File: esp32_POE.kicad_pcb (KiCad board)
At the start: 2 copper layers, 204.8 x 25 mm, 68 parts, among them IC1 TPS2373-4RGWR, J1 USB_C_Receptacle_USB2.0_14P, J10 Conn_01x02, J2 WE-RJ45LAN 10/100BaseT PoE, J3 Screw_Terminal_01x03, J4 Screw_Terminal_01x03, J5 Screw_Terminal_01x03, J6 Screw_Terminal_01x03, J7 Conn_01x04, J8 Conn_01x02, J9 Conn_01x04, Q1 NPN, Q2 NPN, SW1 SW_Push, U1 ESP32-WROOM-32E, U2 CH340C, U4 LAN8710A, U5 AMS1117-3.3, U7 TXS0108EPW

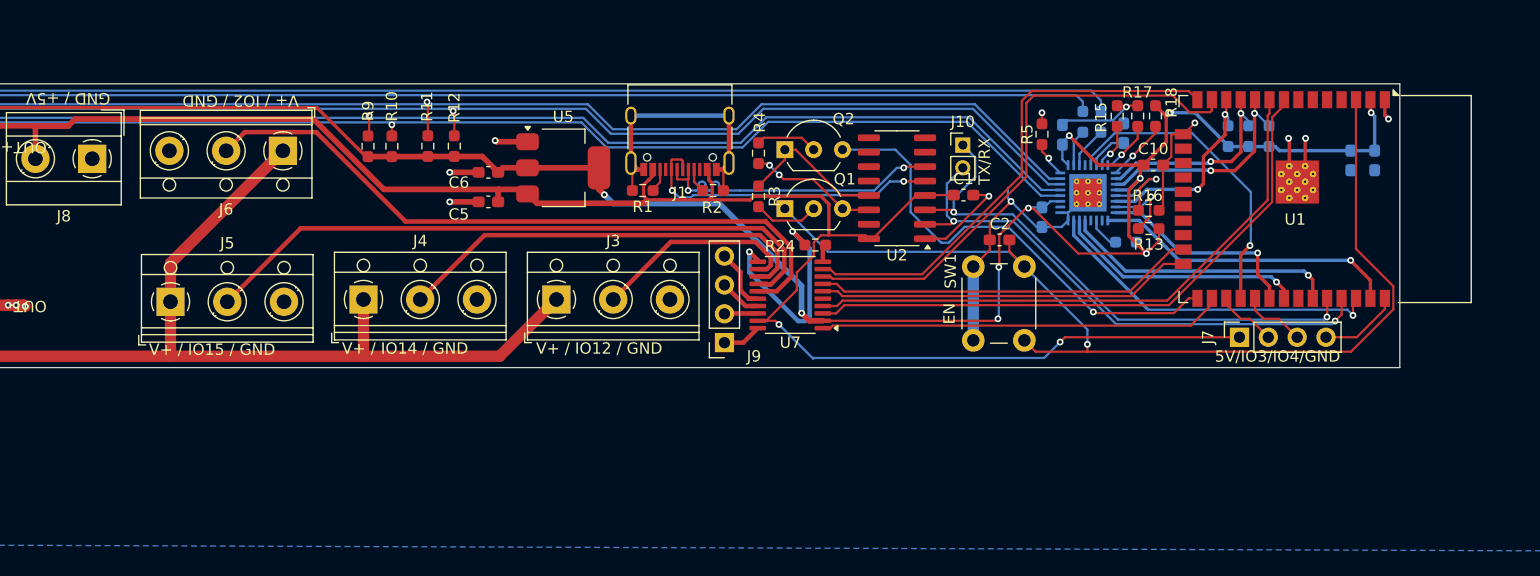
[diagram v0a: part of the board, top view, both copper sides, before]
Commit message: Modified schematic : fixed esp32 circuit, changed to SN74 level shifter, changed to LAN8270
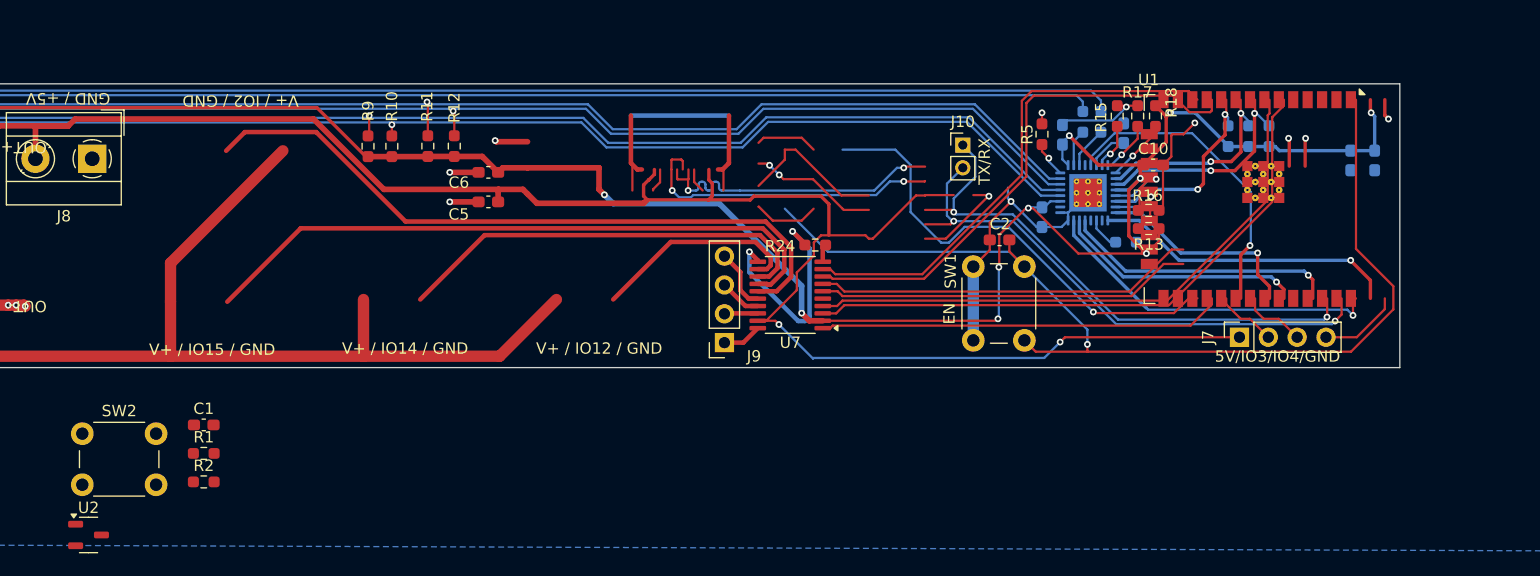
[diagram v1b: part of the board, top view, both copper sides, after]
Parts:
- removed J1: USB_C_Receptacle_USB2.0_14P, Connector_USB:USB_C_Receptacle_XKB_U262-16XN-4BVC11
- removed J3, J4, J5, J6: Screw_Terminal_01x03, TerminalBlock_RND:TerminalBlock_RND_205-00013_1x03_P5.00mm_Horizontal
- removed Q1, Q2: NPN, Package_TO_SOT_THT:TO-92_Inline_Wide
- removed R3, R4: 10k, Resistor_SMD:R_0603_1608Metric_Pad0.98x0.95mm_HandSolder
- removed U5: AMS1117-3.3, Package_TO_SOT_SMD:SOT-223-3_TabPin2
- added SW2: SW_Push, Button_Switch_THT:SW_PUSH_6mm_H4.3mm, F.Cu at (149.6, 149.8)
- C1: value 100nF -> 2.2uF
- C5, C6: value 10uF -> 1uF
- R1, R2: value 5.1k -> 10k
- U1: footprint RF_Module:ESP32-WROOM-32D -> RF_Module:ESP32-WROOM-32E
- U2: value CH340C -> XC6206PxxxMR; footprint Package_SO:SOIC-16_3.9x9.9mm_P1.27mm -> Package_TO_SOT_SMD:SOT-23-3
- moved U2 77.5 mm to (150.2, 158.7), turned to 0 degrees
- moved C1 69.9 mm to (160.3, 149.1)
- moved R2 51.7 mm to (160.3, 154.1)
- moved R1 45.1 mm to (160.3, 151.6), turned to 0 degrees
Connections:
- C1 pad 1: +5V -> IO0
- R1 pad 1: Net-(J1-CC2) -> +3.3V
- R1 pad 2: GND -> IO0
- R2 pad 1: Net-(J1-CC1) -> +3.3V
- R2 pad 2: GND -> EN
- U2 pad 2: TX -> +3.3V
- U2 pad 3: RX -> +5V
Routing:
- net (no net): track 0.00 -> 95.5 mm, vias 0 -> 6
- net D+: track 27.6 -> 0.00 mm, vias 2 -> 0
- net D-: track 27.6 -> 0.00 mm, vias 2 -> 0
- net Net-(Q2-C): track 13.2 -> 0.00 mm
- net Net-(Q1-E): track 11.4 -> 0.00 mm, vias 2 -> 0
- net Net-(Q1-B): track 5.80 -> 0.00 mm
- net Net-(Q2-B): track 5.48 -> 0.00 mm
- net Net-(J1-CC1): track 2.17 -> 0.00 mm
- net Net-(J1-CC2): track 2.11 -> 0.00 mm

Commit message: Finished setting up the schematic, started basic routing
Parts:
- removed the C17 at (106.0, 133.0)
- removed IC1: TPS2373-4RGWR, Package_DFN_QFN:Texas_RGW0020A_VQFN-20-1EP_5x5mm_P0.65mm_EP3.15x3.15mm
- removed J10: Conn_01x02, Connector_PinHeader_2.00mm:PinHeader_1x02_P2.00mm_Vertical
- removed the R35 at (100.0, 139.0)
- removed the R36 at (97.9, 139.0)
- removed R37: 1.3k, Resistor_THT:R_Axial_DIN0207_L6.3mm_D2.5mm_P10.16mm_Horizontal
- removed the U7 at (212.0, 137.6)
- added C1: 10uF, Capacitor_SMD:C_0603_1608Metric, F.Cu at (105.7, 120.0)
- added C14: 22uF/35V, Capacitor_SMD:C_0805_2012Metric, F.Cu at (135.5, 111.8)
- added C15: .1uF, Capacitor_SMD:C_0603_1608Metric, F.Cu at (110.1, 106.4)
- added C3: 4.7uF,100V, Capacitor_SMD:C_1206_3216Metric, F.Cu at (125.5, 123.3)
- added C4: .1uF, Capacitor_SMD:C_0603_1608Metric, F.Cu at (125.6, 131.3)
- added C5: 4.7uF,100V, Capacitor_SMD:C_1206_3216Metric, F.Cu at (128.8, 123.3)
- added C6: .1uF, Capacitor_SMD:C_0603_1608Metric, F.Cu at (113.3, 111.1)
- added D1: LED, LED_SMD:LED_0603_1608Metric, F.Cu at (82.9, 142.0)
- added D3: 51V, Diode_SMD:D_SMA, F.Cu at (113.4, 119.9)
- added D5: SDT20B100D1-13, Package_TO_SOT_SMD:TO-252-2, F.Cu at (137.5, 117.3)
- added D6: LED, LED_SMD:LED_0603_1608Metric, F.Cu at (120.8, 142.3)
- added D7: LED, LED_SMD:LED_0603_1608Metric, F.Cu at (123.4, 142.3)
- added J1: Barrel_Jack_Switch, Connector_BarrelJack:BarrelJack_Horizontal, F.Cu at (90.3, 130.0)
- added J4: Conn_01x04, Connector_PinSocket_1.27mm:PinSocket_1x04_P1.27mm_Vertical, F.Cu at (256.7, 142.0)
- added J5: Conn_01x03, Connector_JST:JST_XH_B3B-XH-AM_1x03_P2.50mm_Vertical, F.Cu at (199.1, 124.9)
- added J6: Conn_01x03, Connector_JST:JST_XH_B3B-XH-AM_1x03_P2.50mm_Vertical, F.Cu at (187.0, 135.0)
- added L1: SMMS1770-330M, Inductor_SMD:L_Vishay_IHLP-6767, F.Cu at (151.1, 114.8)
- added R1: 3k, Resistor_SMD:R_0603_1608Metric, F.Cu at (84.6, 142.0)
- added R2: 10k, Resistor_SMD:R_0603_1608Metric, F.Cu at (120.2, 69.6)
- added R21: 53.6k, Resistor_SMD:R_0603_1608Metric, F.Cu at (158.2, 127.0)
- added R22: 10.2k, Resistor_SMD:R_0603_1608Metric, F.Cu at (140.7, 129.1)
- added R23: 143k, Resistor_SMD:R_0603_1608Metric, F.Cu at (158.2, 129.3)
- added R25: 3k, Resistor_SMD:R_0603_1608Metric, F.Cu at (120.8, 139.3)
- added R26: 10, Resistor_SMD:R_0603_1608Metric, F.Cu at (219.7, 127.9)
- added R27: 10, Resistor_SMD:R_0603_1608Metric, F.Cu at (219.7, 130.4)
- added R28: 10, Resistor_SMD:R_0603_1608Metric, F.Cu at (219.7, 132.9)
- added R3: 118k, Resistor_SMD:R_0603_1608Metric, F.Cu at (131.7, 125.8)
- added R4: 36.5k, Resistor_SMD:R_0603_1608Metric, F.Cu at (131.7, 128.9)
- added U1: HY931147C, HY931147C:HY931147C, F.Cu at (107.2, 133.0)
- added U2: TPS2372, Package_DFN_QFN:Texas_RGW0020A_VQFN-20-1EP_5x5mm_P0.65mm_EP3.15x3.15mm, F.Cu at (130.0, 134.6)
- added U5: SN74LVC8T245, Package_SO:TSSOP-24_4.4x7.8mm_P0.65mm, F.Cu at (229.3, 132.5)
- C10: footprint Capacitor_SMD:C_0603_1608Metric_Pad1.08x0.95mm_HandSolder -> Capacitor_SMD:C_0603_1608Metric
- C11: value 10uF -> 470pF; footprint Capacitor_THT:CP_Radial_D5.0mm_P2.50mm -> Capacitor_SMD:C_0603_1608Metric
- C12: value 10uF -> 22uF/35V; footprint Capacitor_SMD:C_0603_1608Metric_Pad1.08x0.95mm_HandSolder -> Capacitor_SMD:C_0805_2012Metric; moved to F.Cu
- C13: value 10uF -> .1uF; footprint Capacitor_SMD:C_0603_1608Metric_Pad1.08x0.95mm_HandSolder -> Capacitor_SMD:C_0603_1608Metric
- C16: value .1uF -> 22uF/35V; footprint Capacitor_SMD:C_0603_1608Metric_Pad1.08x0.95mm_HandSolder -> Capacitor_SMD:C_0805_2012Metric
- C17: renamed from C3; footprint Capacitor_SMD:C_0603_1608Metric_Pad1.08x0.95mm_HandSolder -> Capacitor_SMD:C_0603_1608Metric
- C18: renamed from C4; footprint Capacitor_SMD:C_0603_1608Metric_Pad1.08x0.95mm_HandSolder -> Capacitor_SMD:C_0603_1608Metric
- C19: renamed from C5; footprint Capacitor_SMD:C_0603_1608Metric_Pad1.08x0.95mm_HandSolder -> Capacitor_SMD:C_0603_1608Metric
- C2: renamed from C14; footprint Capacitor_SMD:C_0603_1608Metric_Pad1.08x0.95mm_HandSolder -> Capacitor_SMD:C_0603_1608Metric
- C20: renamed from C6; footprint Capacitor_SMD:C_0603_1608Metric_Pad1.08x0.95mm_HandSolder -> Capacitor_SMD:C_0603_1608Metric
- C21: renamed from C2; footprint Capacitor_SMD:C_0603_1608Metric_Pad1.08x0.95mm_HandSolder -> Capacitor_SMD:C_0603_1608Metric
- C22: renamed from C1; footprint Capacitor_SMD:C_0603_1608Metric_Pad1.08x0.95mm_HandSolder -> Capacitor_SMD:C_0603_1608Metric
- C7: value 1uF -> 56pF; footprint Capacitor_SMD:C_0603_1608Metric_Pad1.08x0.95mm_HandSolder -> Capacitor_SMD:C_0603_1608Metric; moved to F.Cu
- C8: value .1uF -> 1200pF; footprint Capacitor_SMD:C_0603_1608Metric_Pad1.08x0.95mm_HandSolder -> Capacitor_SMD:C_0603_1608Metric
- C9: value 1uF -> .1uF,10V; footprint Capacitor_SMD:C_0603_1608Metric_Pad1.08x0.95mm_HandSolder -> Capacitor_SMD:C_0603_1608Metric; moved to F.Cu
- D2: value SMAJ58A -> SDT20B100D1-13; footprint Diode_SMD:D_SMA -> Package_TO_SOT_SMD:TO-252-2
- D4: value 1N4742-12V -> LED; footprint Diode_THT:D_DO-41_SOD81_P10.16mm_Horizontal -> LED_SMD:LED_0603_1608Metric
- J2: value WE-RJ45LAN 10/100BaseT PoE -> Conn_02x03_Odd_Even; footprint custom:7499211125 -> Connector_PinHeader_2.54mm:PinHeader_2x03_P2.54mm_Vertical
- J7: value Conn_01x04 -> Conn_01x03; footprint Connector_PinSocket_2.54mm:PinSocket_1x04_P2.54mm_Vertical -> Connector_JST:JST_XH_B3B-XH-AM_1x03_P2.50mm_Vertical
- J8: value Conn_01x02 -> Conn_01x03; footprint TerminalBlock_MetzConnect:TerminalBlock_MetzConnect_Type055_RT01502HDWU_1x02_P5.00mm_Horizontal -> Connector_JST:JST_XH_B3B-XH-AM_1x03_P2.50mm_Vertical
- R10: value 10k -> 63.4; footprint Resistor_SMD:R_0603_1608Metric_Pad0.98x0.95mm_HandSolder -> Resistor_SMD:R_0603_1608Metric
- R11: value 10k -> 90.9; footprint Resistor_SMD:R_0603_1608Metric_Pad0.98x0.95mm_HandSolder -> Resistor_SMD:R_0603_1608Metric
- R12: value 10k -> 49.9k; footprint Resistor_SMD:R_0603_1608Metric_Pad0.98x0.95mm_HandSolder -> Resistor_SMD:R_0603_1608Metric
- R13, R15, R16, R17: value 3k -> 10; footprint Resistor_SMD:R_0603_1608Metric_Pad0.98x0.95mm_HandSolder -> Resistor_SMD:R_0603_1608Metric
- R14: value 3k -> 10; footprint Resistor_SMD:R_0603_1608Metric_Pad0.98x0.95mm_HandSolder -> Resistor_SMD:R_0603_1608Metric; moved to F.Cu
- R18: value 3k -> 12k; footprint Resistor_SMD:R_0603_1608Metric_Pad0.98x0.95mm_HandSolder -> Resistor_SMD:R_0603_1608Metric
- R19, R20: footprint Resistor_SMD:R_0603_1608Metric_Pad0.98x0.95mm_HandSolder -> Resistor_SMD:R_0603_1608Metric; moved to F.Cu
- R24: value 12.1k -> 294k; footprint Resistor_SMD:R_0603_1608Metric_Pad0.98x0.95mm_HandSolder -> Resistor_SMD:R_0603_1608Metric
- R29: value 18k -> 10; footprint Resistor_SMD:R_0603_1608Metric_Pad0.98x0.95mm_HandSolder -> Resistor_SMD:R_0603_1608Metric
- R30: value 7.5k -> 10; footprint Resistor_SMD:R_0603_1608Metric_Pad0.98x0.95mm_HandSolder -> Resistor_SMD:R_0603_1608Metric
- R31: value 62 -> 10; footprint Resistor_SMD:R_0603_1608Metric_Pad0.98x0.95mm_HandSolder -> Resistor_SMD:R_0603_1608Metric
- R32: value 1k -> 10; footprint Resistor_SMD:R_0603_1608Metric_Pad0.98x0.95mm_HandSolder -> Resistor_SMD:R_0603_1608Metric
- R33: value 1 -> 10; footprint Resistor_SMD:R_0603_1608Metric_Pad0.98x0.95mm_HandSolder -> Resistor_SMD:R_0603_1608Metric
- R34: footprint Resistor_SMD:R_0603_1608Metric_Pad0.98x0.95mm_HandSolder -> Resistor_SMD:R_0603_1608Metric
- R35: renamed from R2; footprint Resistor_SMD:R_0603_1608Metric_Pad0.98x0.95mm_HandSolder -> Resistor_SMD:R_0603_1608Metric
- R36: renamed from R1; footprint Resistor_SMD:R_0603_1608Metric_Pad0.98x0.95mm_HandSolder -> Resistor_SMD:R_0603_1608Metric
- R5: value 12k -> 3k; footprint Resistor_SMD:R_0603_1608Metric_Pad0.98x0.95mm_HandSolder -> Resistor_SMD:R_0603_1608Metric
- R6: value 300 -> 25k; footprint Resistor_SMD:R_0603_1608Metric_Pad0.98x0.95mm_HandSolder -> Resistor_SMD:R_0603_1608Metric; moved to F.Cu
- R7: value 12k -> 13.3k; footprint Resistor_SMD:R_0603_1608Metric_Pad0.98x0.95mm_HandSolder -> Resistor_SMD:R_0603_1608Metric; moved to F.Cu
- R8: value 300 -> 220k; footprint Resistor_SMD:R_0603_1608Metric_Pad0.98x0.95mm_HandSolder -> Resistor_SMD:R_0603_1608Metric; moved to F.Cu
- R9: value 10k -> 3k; footprint Resistor_SMD:R_0603_1608Metric_Pad0.98x0.95mm_HandSolder -> Resistor_SMD:R_0603_1608Metric
- SW1, SW2: footprint Button_Switch_THT:SW_PUSH_6mm_H4.3mm -> Button_Switch_SMD:SW_Push_SPST_NO_Alps_SKRK
- U3: value ~ -> TPS54560BDDA; footprint custom:Mini_DC-DC_Buck -> Package_SO:Texas_R-PDSO-G8_EP2.95x4.9mm_Mask2.4x3.1mm_ThermalVias
- U4: value LAN8710A -> LAN8720A; footprint Package_DFN_QFN:QFN-32-1EP_5x5mm_P0.5mm_EP3.3x3.3mm_ThermalVias -> Package_DFN_QFN:VQFN-24-1EP_4x4mm_P0.5mm_EP2.5x2.5mm_ThermalVias; moved to F.Cu
- moved C10 142.6 mm to (102.2, 110.6)
- moved R14 142.1 mm to (120.2, 67.1), turned to 0 degrees
- moved R13 140.5 mm to (120.2, 64.6)
- moved R20 138.1 mm to (116.7, 136.2)
- moved R19 134.7 mm to (118.3, 136.2)
- moved U4 132.3 mm to (107.2, 110.8), turned to 180 degrees
- moved R16 130.3 mm to (128.3, 69.6)
- moved R17 127.9 mm to (128.3, 64.6), turned to 0 degrees
- moved R29 125.7 mm to (219.7, 135.4), turned to 180 degrees
- moved R18 125.2 mm to (128.3, 74.6), turned to 0 degrees
- moved R15 125.2 mm to (128.3, 67.1), turned to 0 degrees
- moved R31 122.5 mm to (210.1, 135.8), turned to 180 degrees
- moved R33 120.7 mm to (210.1, 138.9), turned to 180 degrees
- moved R5 117.7 mm to (128.3, 72.1), turned to 0 degrees
- moved SW2 117.7 mm to (259.5, 107.6), turned to 180 degrees
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- renumbered J9 to J3, U1 to U6, U2 to U7
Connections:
- net CLK renamed /ETH_CLK
- C10 pad 1: +3.3V -> GND
- C10 pad 2: GND -> +3.3V
- C11 pad 1: V+ -> +3.3V
- C12 pad 1: GND -> VCC
- C12 pad 2: +3.3V -> GND
- C13 pad 1: GND -> +3.3V
- C13 pad 2: +3.3V -> GND
- C16 pad 1: Net-(D4-A) -> VCC
- C19 pad 1: +5V -> VCC
- C7 pad 1: Net-(U4-VDDCR) -> GND
- C7 pad 2: GND -> Net-(U3-COMP)
- C8 pad 1: V+ -> GND
- C8 pad 2: V- -> Net-(C8-Pad2)
- C9 pad 1: +3.3V -> Net-(D5-K)
- C9 pad 2: GND -> Net-(U3-BOOT)
- D2 pad 1: V+ -> Net-(D1-A)
- D2 pad 2: V- -> /POE_V+
- D4 pad 1: V+ -> Net-(D4-K)
- D4 pad 2: Net-(D4-A) -> /POE_V+
- J2 pad 1: RD+ -> FB
- J2 pad 2: RD- -> Net-(J2-Pin_2)
- J2 pad 3: +3.3V -> FB
- J2 pad 4: TD+ -> Net-(J2-Pin_4)
- J2 pad 5: +3.3V -> FB
- J2 pad 6: TD- -> Net-(J2-Pin_6)
- J3 pad 4: Net-(J9-Pin_4) -> Net-(J3-Pin_4)
- J7 pad 1: +5V -> GND
- J7 pad 2: GPIOOUT3 -> Net-(J7-Pin_2)
- J7 pad 3: GPIOOUT4 -> VCC
- J8 pad 2: +5V -> Net-(J8-Pin_2)
- R10 pad 1: +3.3V -> /POE_V-
- R10 pad 2: TD- -> Net-(U2-CLSA)
- R11 pad 1: +3.3V -> Net-(U2-CLSB)
- R11 pad 2: RD+ -> /POE_V-
- R12 pad 1: +3.3V -> Net-(U2-REF)
- R12 pad 2: RD- -> /POE_V-
- R13 pad 1: Net-(U4-COL/CRS_DV/~{MODE2}) -> /ETH_RXD0
- R13 pad 2: +3.3V -> Net-(U4-RXD0/MODE0)
- R14 pad 1: IO27 -> Net-(U4-RXD1/MODE1)
- R14 pad 2: +3.3V -> /ETH_RXD1
- R15 pad 1: Net-(U4-RXCLK/~{PHYAD1}) -> Net-(U4-CRS_DV/MODE2)
- R15 pad 2: GND -> /ETH_CRS
- R16 pad 1: Net-(U4-RXER/RXD4/~{PHYAD0}) -> Net-(U4-MDIO)
- R16 pad 2: GND -> /ETH_MDIO
- R17 pad 1: Net-(U4-RXD3/~{PHYAD2}) -> Net-(U4-RXER/PHYAD0)
- R17 pad 2: GND -> +3.3V
- R18 pad 1: Net-(U4-RXD2/~{RMIISEL}) -> GND
- R18 pad 2: +3.3V -> Net-(U4-RBIAS)
- R19 pad 1: IO26 -> Net-(U4-LED1/REGOFF)
- R19 pad 2: +3.3V -> /LED1/REGOFF
- R20 pad 1: IO25 -> Net-(U4-LED2/~{INTSEL})
- R20 pad 2: +3.3V -> /LED2/nINTSEL
- R24 pad 1: Net-(U7-OE) -> Net-(J2-Pin_6)
- R24 pad 2: GND -> VCC
- R29 pad 1: Net-(R29-Pad1) -> /5V_CHANNEL5
- R29 pad 2: V+ -> Net-(J3-Pin_4)
- R30 pad 1: Net-(IC1-DEN) -> /5V_CHANNEL4
- R30 pad 2: Net-(R29-Pad1) -> Net-(J5-Pin_2)
- R31 pad 1: V- -> /5V_CHANNEL3
- R31 pad 2: Net-(R31-Pad2) -> Net-(J6-Pin_2)
- R32 pad 1: Net-(IC1-CLSB) -> /5V_CHANNEL2
- R32 pad 2: V- -> Net-(J7-Pin_2)
- R33 pad 1: Net-(IC1-CLSA) -> /5V_CHANNEL1
- R33 pad 2: Net-(R31-Pad2) -> Net-(J8-Pin_2)
- R34 pad 1: Net-(IC1-CLSB) -> GND
- R34 pad 2: V- -> Net-(D7-K)
- R5 pad 1: GND -> +3.3V
- R5 pad 2: Net-(U4-RBIAS) -> /ETH_MDIO
- R6 pad 1: LED1 -> /POE_V+
- R6 pad 2: Net-(U4-LED1/~{REGOFF}) -> Net-(U2-DEN)
- R7 pad 1: Net-(U4-~{RST}) -> Net-(U3-COMP)
- R7 pad 2: +3.3V -> Net-(C8-Pad2)
- R8 pad 1: Net-(U4-LED2/~{INTSEL}) -> Net-(U3-RT/CLK)
- R8 pad 2: LED2 -> GND
- R9 pad 1: +3.3V -> Net-(U2-TPH)
- R9 pad 2: TD+ -> Net-(D4-K)
- U3 pad 1: V+ -> Net-(U3-BOOT)
- U3 pad 2: GND -> /POE_V+
- U3 pad 3: +5V -> Net-(U3-EN)
- U3 pad 4: GND -> Net-(U3-RT/CLK)
- U4 pad 10: IO26 -> Net-(U4-RXER/PHYAD0)
- U4 pad 11: IO25 -> Net-(U4-CRS_DV/MODE2)
- U4 pad 12: +3.3V -> Net-(U4-MDIO)
- U4 pad 13: Net-(U4-RXER/RXD4/~{PHYAD0}) -> /ETH_MDC
- U4 pad 14: IO27 -> unconnected-(U4-~{INT}/REFCLKO-Pad14)
- U4 pad 15: Net-(U4-COL/CRS_DV/~{MODE2}) -> /ETH_RST
- U4 pad 16: IO18 -> /ETH_TXDEN
- U4 pad 17: IO23 -> /ETH_TXD0
- U4 pad 18: unconnected-(U4-~{INT}/TXER/TXD4-Pad18) -> /ETH_TXD1
- U4 pad 19: Net-(U4-~{RST}) -> +3.3V
- U4 pad 20: unconnected-(U4-TXCLK-Pad20) -> /TX-
- U4 pad 21: IO21 -> /TX+
- U4 pad 22: IO19 -> /RX-
- U4 pad 23: IO22 -> /RX+
- U4 pad 24: GND -> Net-(U4-RBIAS)
- U4 pad 3: Net-(U4-LED1/~{REGOFF}) -> Net-(U4-LED1/REGOFF)
- U4 pad 6: Net-(U4-VDDCR) -> +3.3V
- U4 pad 7: Net-(U4-RXCLK/~{PHYAD1}) -> Net-(U4-RXD1/MODE1)
- U4 pad 8: Net-(U4-RXD3/~{PHYAD2}) -> Net-(U4-RXD0/MODE0)
- U4 pad 9: Net-(U4-RXD2/~{RMIISEL}) -> +3.3V
- U6 pad 10: IO25 -> /ETH_RXD0
- U6 pad 11: IO26 -> /ETH_RXD1
- U6 pad 12: IO27 -> /ETH_CRS
- U6 pad 13: CHANNEL3 -> /CHANNEL4
- U6 pad 14: CHANNEL4 -> /CHANNEL3
- U6 pad 23: CHANNEL2 -> /CHANNEL5
- U6 pad 24: CHANNEL1 -> /ETH_RST
- U6 pad 26: BRKOUT4 -> /CHANNEL1
- U6 pad 27: GPIOOUT3 -> /CHANNEL6
- U6 pad 29: GPIOOUT4 -> /CHANNEL2
- U6 pad 30: IO18 -> /ETH_MDIO
- U6 pad 31: IO19 -> /ETH_TXD0
- U6 pad 33: IO21 -> /ETH_TXDEN
- U6 pad 36: IO22 -> /ETH_TXD1
- U6 pad 37: IO23 -> /ETH_MDC
- U6 pad 8: BRKOUT3 -> /CHANNEL7
- U6 pad 9: BRKOUT2 -> /CHANNEL8
- U7 pad 3: +5V -> VCC
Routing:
- net +3.3V: track 257.1 -> 0.00 mm, vias 10 -> 0
- net LED1: track 190.9 -> 0.00 mm
- net LED2: track 173.4 -> 0.00 mm
- net V+: track 172.2 -> 0.00 mm
- net TD+: track 170.3 -> 0.00 mm, vias 1 -> 0
- net RD+: track 169.7 -> 0.00 mm, vias 1 -> 0
- net TD-: track 167.6 -> 0.00 mm, vias 1 -> 0
- net RD-: track 166.7 -> 0.00 mm, vias 1 -> 0
- net +5V: track 163.6 -> 0.00 mm, vias 2 -> 0
- net GND: track 158.3 -> 0.00 mm, vias 17 -> 4
- net (no net): track 95.5 -> 0.00 mm, vias 6 -> 0
- net EN: track 90.2 -> 0.00 mm, vias 1 -> 0
- net V-: track 60.8 -> 0.00 mm
- net Net-(J5-Pin_2): track 60.7 -> 0.00 mm
- net Net-(J4-Pin_2): track 57.2 -> 0.00 mm
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- added copper zone on F.Cu, net /POE_V+
- added copper zone on F.Cu, net GND
- added copper zone on In1.Cu, net GND
- added copper zone on F.Cu, net VCC
- added copper zone on In2.Cu, net VCC
- removed copper zone on B.Cu, net GND
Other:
- board size 204.8 x 25 mm -> 204.8 x 40 mm
- copper layers 2 -> 4
- board text removed: "5V/IO3/IO4/GND"
- board text removed: "EN"
- board text removed: "GND / +5V"
- board text removed: "IO4/IO32/IO33/NC"
- board text removed: "TX/RX"
- board text removed: "V+ / IO12 / GND"
- board text removed: "V+ / IO14 / GND"
- board text removed: "V+ / IO15 / GND"
- board text removed: "V+ / IO2 / GND"

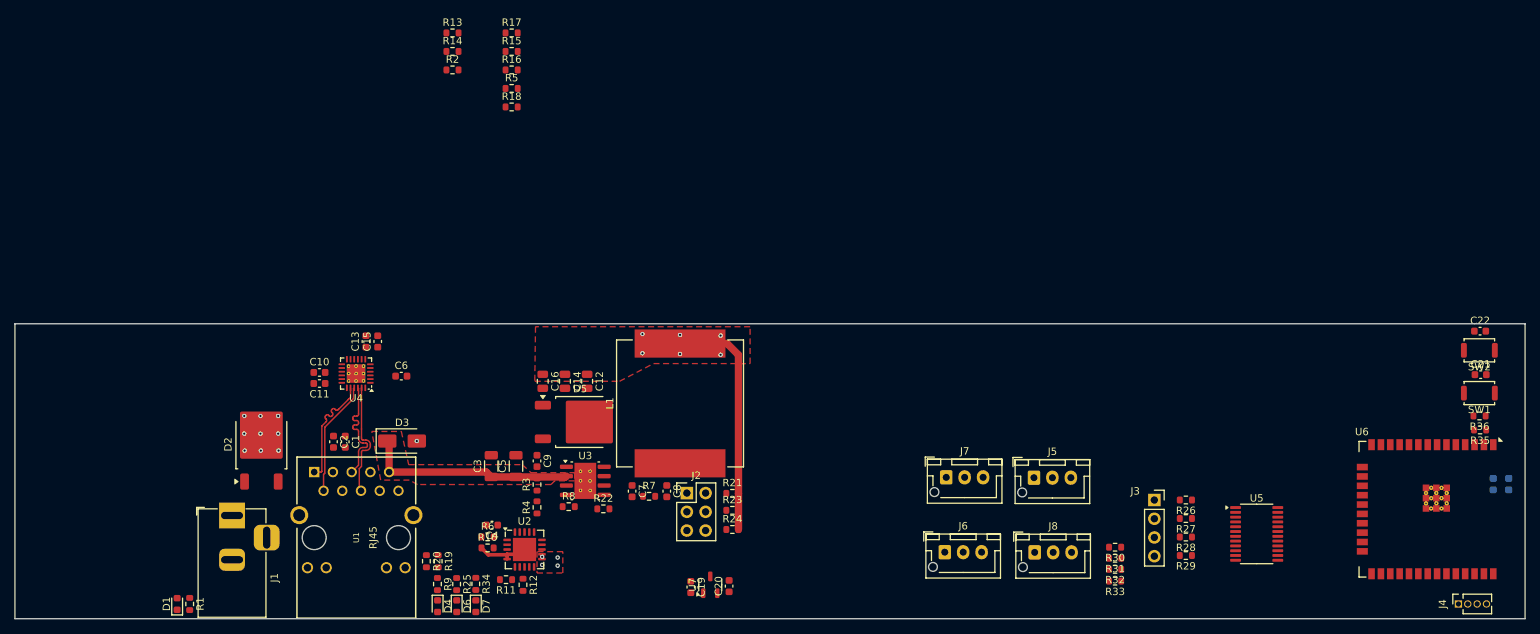
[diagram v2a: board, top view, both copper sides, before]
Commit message: Finished up roughing pass, reduced pcb size
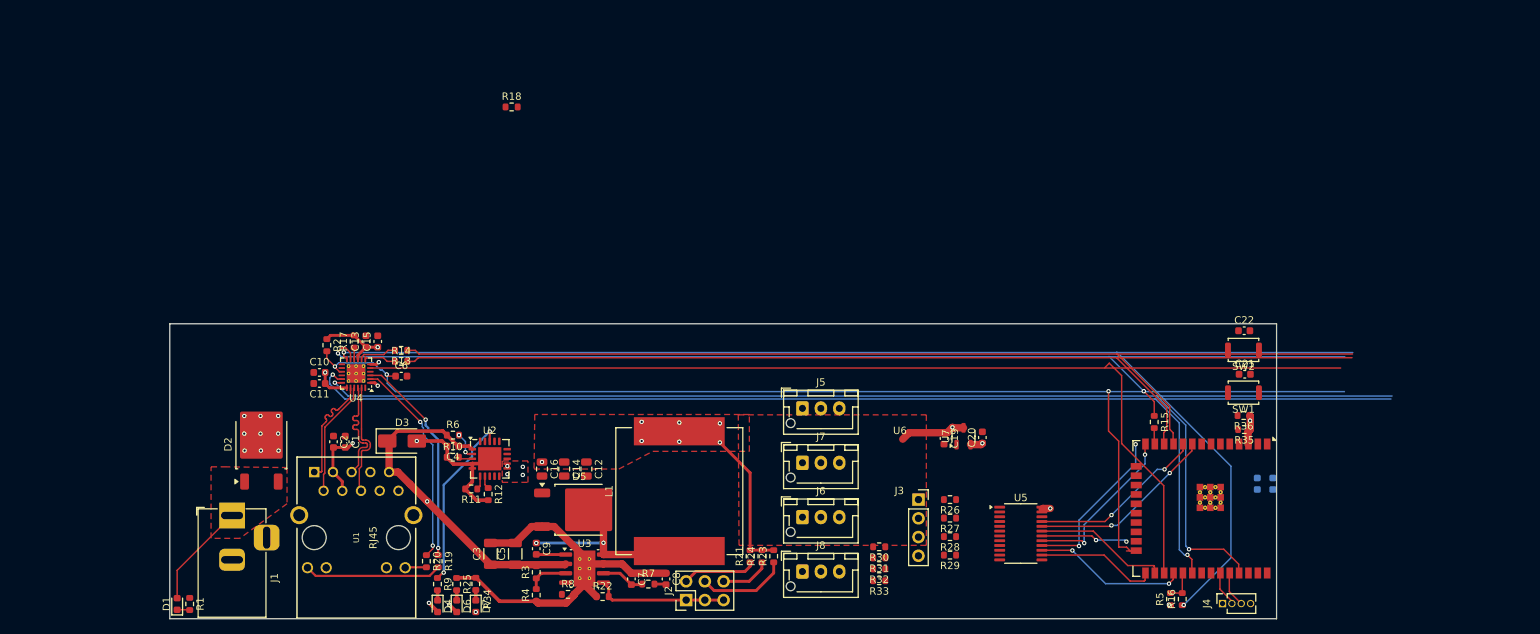
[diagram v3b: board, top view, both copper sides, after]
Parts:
- moved R16 115.9 mm to (219.2, 141.3), turned to 90 degrees
- moved R5 113.0 mm to (217.6, 141.3), turned to 90 degrees
- moved R15 100.6 mm to (215.4, 117.3), turned to -90 degrees
- moved R17 47.0 mm to (106.9, 106.4), turned to 90 degrees
- moved R13 43.6 mm to (113.3, 107.6), turned to 180 degrees
- moved R14 42.6 mm to (113.3, 109.1)
- moved R2 41.0 mm to (103.2, 106.9), turned to -90 degrees
- moved U7 39.8 mm to (189.5, 119.2)
- moved C19 39.8 mm to (186.9, 119.5)
- moved C20 39.8 mm to (192.1, 119.4)
- moved J5 32.8 mm to (167.7, 115.5)
- moved J4 32.0 mm to (224.7, 141.9)
- moved C17 32.0 mm to (229.4, 125.7)
- moved C18 32.0 mm to (231.5, 125.7)
- moved C21 32.0 mm to (227.7, 110.8)
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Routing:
- net +3.3V: track 0.00 -> 232.8 mm, vias 0 -> 10
- net Net-(U4-MDIO): track 0.00 -> 181.5 mm, vias 0 -> 2
- net /ETH_TXD1: track 0.00 -> 176.6 mm, vias 0 -> 2
- net /ETH_TXD0: track 0.00 -> 173.7 mm, vias 0 -> 2
- net /ETH_RST: track 0.00 -> 168.6 mm, vias 0 -> 3
- net /ETH_CLK: track 0.00 -> 164.0 mm
- net Net-(U4-CRS_DV/MODE2): track 0.00 -> 150.6 mm, vias 0 -> 2
- net /ETH_RXD0: track 0.00 -> 143.9 mm
- net /ETH_RXD1: track 0.00 -> 143.2 mm
- net GND: track 0.00 -> 55.3 mm
- net /POE_V+: track 44.9 -> 78.4 mm, vias 9 -> 11
- net Net-(U4-LED1/REGOFF): track 0.00 -> 29.1 mm, vias 0 -> 2
- net Net-(U4-LED2/~{INTSEL}): track 0.00 -> 28.3 mm, vias 0 -> 2
- net Net-(D5-K): track 0.00 -> 26.5 mm, vias 0 -> 2
- net /CHANNEL7: track 0.00 -> 25.5 mm, vias 0 -> 2
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- added copper zone on F.Cu, net Net-(D1-A)
- removed copper zone on F.Cu, net /POE_V+
- removed copper zone on In2.Cu, net VCC
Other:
- board size 204.8 x 40 mm -> 150.1 x 40 mm
